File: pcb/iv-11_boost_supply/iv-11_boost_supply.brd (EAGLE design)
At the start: 54.6 x 47 mm, 18 parts, among them IC1 LM555D, M1 IRF540

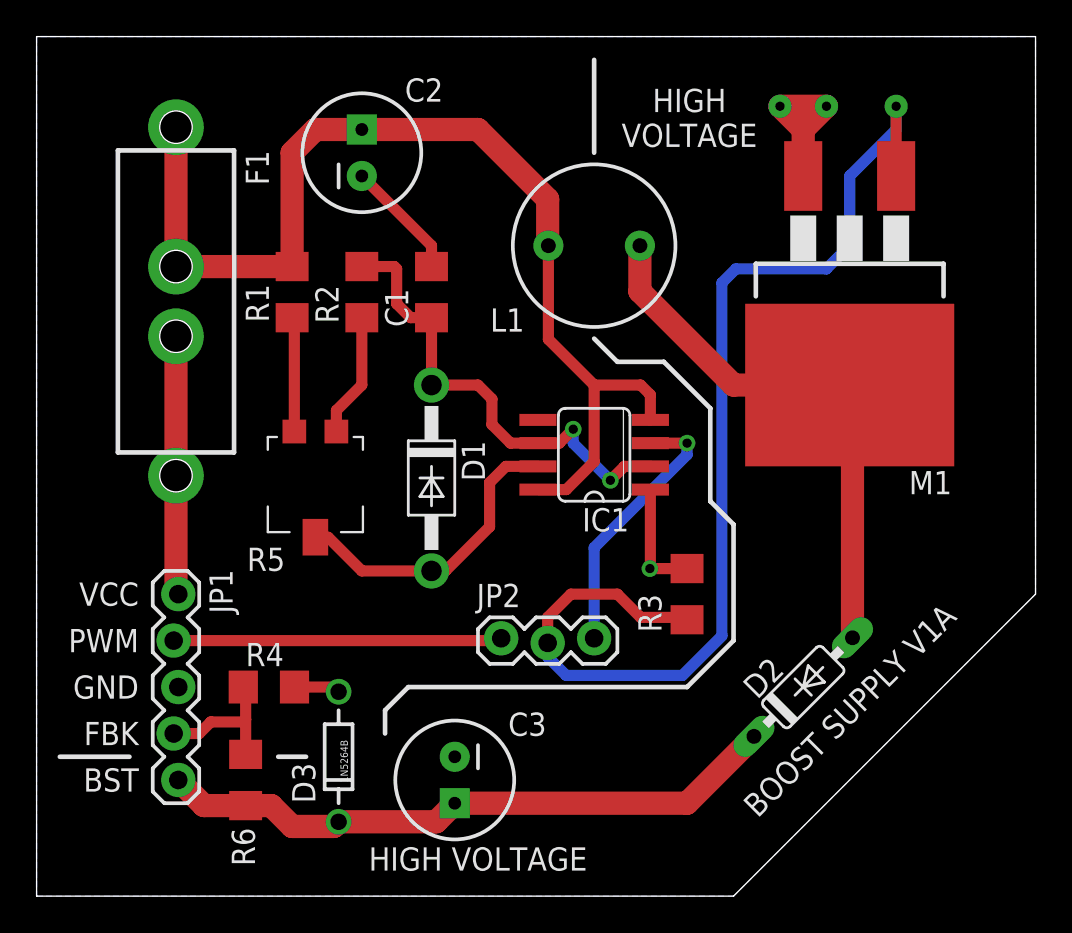
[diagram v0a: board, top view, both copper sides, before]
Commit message: Working on rev B of the boost supply board
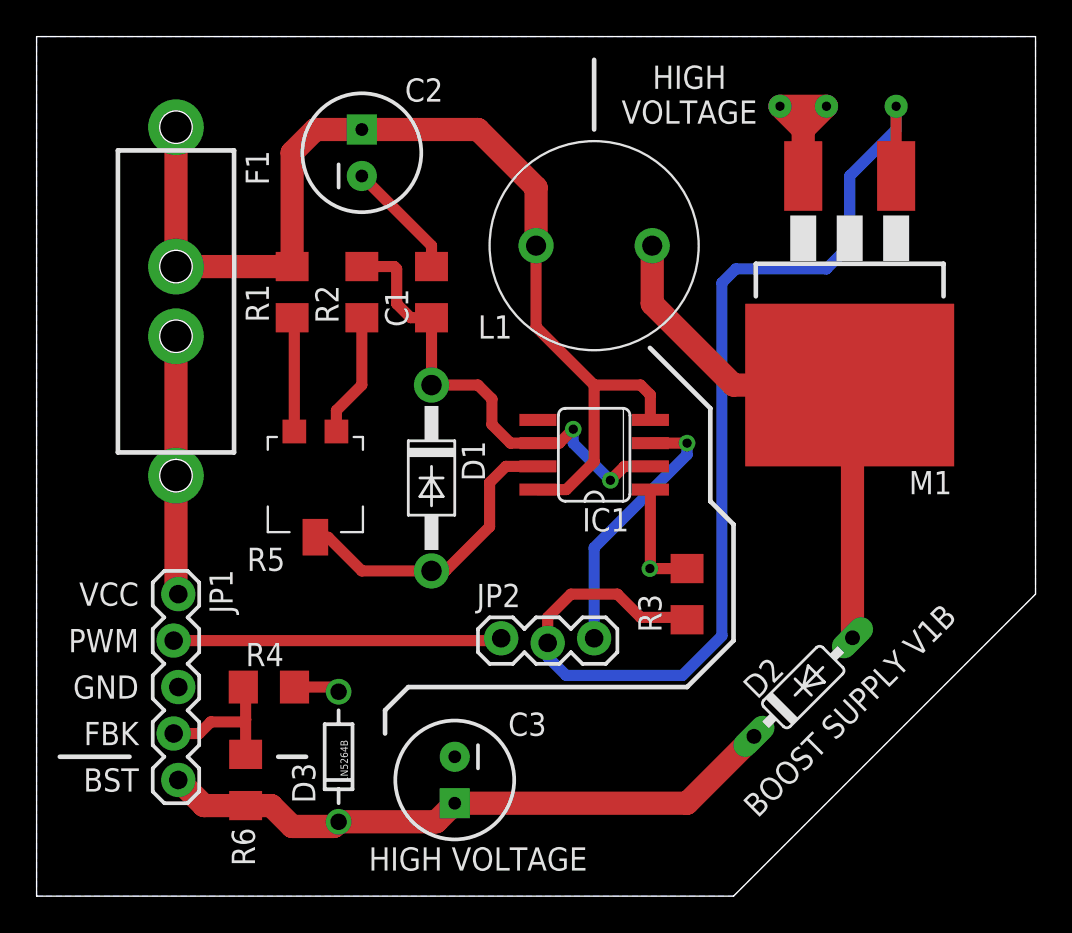
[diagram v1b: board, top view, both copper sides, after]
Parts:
- L1: device SparkFun-Passives:RLB0912 -> boztalay:INDUCTOR-PTH-13MM
- turned L1 to 0 degrees
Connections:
- net N$4: now also L1.B; no longer L1.2
- net VCC_PRC: now also L1.A; no longer L1.1
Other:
- board text added: "BOOST SUPPLY V1B"
- board text removed: "BOOST SUPPLY V1A"
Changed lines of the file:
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@@
 <wire x1="38.1" y1="20.32" x2="36.83" y2="21.59" width="0.254" layer="21"/>
 <wire x1="36.83" y1="21.59" x2="36.83" y2="26.67" width="0.254" layer="21"/>
-<wire x1="36.83" y1="26.67" x2="34.29" y2="29.21" width="0.254" layer="21"/>
-<wire x1="34.29" y1="29.21" x2="31.75" y2="29.21" width="0.254" layer="21"/>
-<wire x1="31.75" y1="29.21" x2="30.48" y2="30.48" width="0.254" layer="21"/>
-<wire x1="30.48" y1="40.64" x2="30.48" y2="45.72" width="0.254" layer="21"/>
+<wire x1="36.83" y1="26.67" x2="33.528" y2="29.972" width="0.254" layer="21"/>
+<wire x1="30.48" y1="41.91" x2="30.48" y2="45.72" width="0.254" layer="21"/>
 <wire x1="0" y1="0" x2="38.1" y2="0" width="0" layer="20"/>
 <wire x1="38.1" y1="0" x2="54.61" y2="16.51" width="0" layer="20"/>
@@
 <text x="5.588" y="8.89" size="1.27" layer="21" font="vector" ratio="11" align="center-right">FBK</text>
 <text x="5.588" y="6.35" size="1.27" layer="21" font="vector" ratio="11" align="center-right">BST</text>
-<text x="35.687" y="42.545" size="1.27" layer="21" font="vector" ratio="11" align="center">HIGH
+<text x="35.687" y="43.815" size="1.27" layer="21" font="vector" ratio="11" align="center">HIGH
 VOLTAGE</text>
 <text x="24.13" y="2.032" size="1.27" layer="21" font="vector" ratio="11" align="center">HIGH VOLTAGE</text>
-<text x="44.45" y="10.16" size="1.27" layer="21" font="vector" ratio="11" rot="R45" align="center">BOOST SUPPLY V1A</text>
+<text x="44.45" y="10.16" size="1.27" layer="21" font="vector" ratio="11" rot="R45" align="center">BOOST SUPPLY V1B</text>
 </plain>
 <attributes>
@@
 <attribute name="VALUE" x="17.018" y="6.223" size="0.4064" layer="21" rot="R90"/>
 </element>
-<element name="F1" library="boztalay" package="1AG-1/4X5/8-FUSE" value="2A/32V" x="7.62" y="32.512" rot="R270"/>
+<element name="F1" library="boztalay" package="1AG-1/4X5/8-FUSE" value="2A/32V" x="7.62" y="32.512" rot="R270">
+<attribute name="RATING" value="" x="7.62" y="32.512" size="1.778" layer="27" rot="R270" display="off"/>
+</element>
 <element name="IC1" library="adafruit" package="SO08" value="LM555D" x="30.48" y="24.13" rot="R90"/>
 <element name="JP1" library="SparkFun-Connectors" package="1X05_LOCK" value="" x="7.62" y="16.51" rot="R270"/>
 <element name="JP2" library="SparkFun-Connectors" package="1X03_LOCK" value="" x="25.4" y="13.97"/>
-<element name="L1" library="SparkFun-Passives" package="RLB0912" value="2200uH" x="30.48" y="35.56" smashed="yes" rot="R180">
-<attribute name="VALUE" x="32.385" y="38.608" size="0.8128" layer="27" rot="R180"/>
-<attribute name="NAME" x="26.67" y="32.131" size="1.27" layer="25" rot="R180"/>
-</element>
 <element name="M1" library="boztalay" package="D2PACK" value="IRF540" x="44.45" y="30.48" rot="R180"/>
 <element name="R1" library="SparkFun-Passives" package="1206" value="100" x="13.97" y="33.02" smashed="yes" rot="R90">
@@
 </element>
 <element name="D2" library="adafruit" package="DO35-7" value="MBR160" x="41.91" y="11.43" rot="R45"/>
+<element name="L1" library="boztalay" package="INDUCTOR-PTH-13MM" value="2200uH" x="30.48" y="35.56" smashed="yes">
+<attribute name="VALUE" x="35.56" y="30.48" size="1.27" layer="27"/>
+<attribute name="NAME" x="24.13" y="30.48" size="1.27" layer="25"/>
+</element>
 </elements>
 <signals>
@@
 </signal>
 <signal name="N$4">
-<contactref element="L1" pad="2"/>
 <contactref element="M1" pad="2"/>
 <contactref element="D2" pad="A"/>
 <wire x1="44.604075" y1="14.124075" x2="44.604075" y2="27.785925" width="1.27" layer="1"/>
 <wire x1="44.604075" y1="27.785925" x2="44.45" y2="27.94" width="1.27" layer="1"/>
-<wire x1="32.9819" y1="35.56" x2="32.9819" y2="33.0581" width="1.27" layer="1"/>
-<wire x1="32.9819" y1="33.0581" x2="38.1" y2="27.94" width="1.27" layer="1"/>
 <wire x1="38.1" y1="27.94" x2="44.45" y2="27.94" width="1.27" layer="1"/>
+<contactref element="L1" pad="B"/>
+<wire x1="33.655" y1="35.56" x2="33.655" y2="32.385" width="1.27" layer="1"/>
+<wire x1="33.655" y1="32.385" x2="38.1" y2="27.94" width="1.27" layer="1"/>
 </signal>
 <signal name="VCC_PRC">
@@
 <contactref element="R1" pad="2"/>
 <contactref element="IC1" pad="4"/>
-<contactref element="L1" pad="1"/>
 <contactref element="IC1" pad="8"/>
 <wire x1="7.62" y1="42.037" x2="7.62" y2="34.417" width="1.27" layer="1"/>
@@
 <wire x1="15.24" y1="41.91" x2="17.78" y2="41.91" width="1.27" layer="1"/>
 <wire x1="17.78" y1="41.91" x2="24.13" y2="41.91" width="1.27" layer="1"/>
-<wire x1="24.13" y1="41.91" x2="27.94" y2="38.1" width="1.27" layer="1"/>
-<wire x1="27.94" y1="38.1" x2="27.94" y2="35.5981" width="1.27" layer="1"/>
-<wire x1="27.94" y1="35.5981" x2="27.9781" y2="35.56" width="1.27" layer="1"/>
-<wire x1="27.9781" y1="35.56" x2="27.9781" y2="30.4419" width="0.6096" layer="1"/>
-<wire x1="27.9781" y1="30.4419" x2="30.48" y2="27.94" width="0.6096" layer="1"/>
 <wire x1="30.48" y1="27.94" x2="33.02" y2="27.94" width="0.6096" layer="1"/>
 <wire x1="33.5534" y1="26.035" x2="33.5534" y2="27.4066" width="0.6096" layer="1"/>
@@
 <wire x1="30.48" y1="23.749" x2="28.956" y2="22.225" width="0.6096" layer="1"/>
 <wire x1="28.956" y1="22.225" x2="27.4066" y2="22.225" width="0.6096" layer="1"/>
+<contactref element="L1" pad="A"/>
+<wire x1="24.13" y1="41.91" x2="27.305" y2="38.735" width="1.27" layer="1"/>
+<wire x1="27.305" y1="38.735" x2="27.305" y2="35.56" width="1.27" layer="1"/>
+<wire x1="27.305" y1="35.56" x2="27.305" y2="31.115" width="0.6096" layer="1"/>
+<wire x1="27.305" y1="31.115" x2="30.48" y2="27.94" width="0.6096" layer="1"/>
 </signal>
 </signals>

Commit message: Finished up rev B of the boost supply board, but the layout still needs to be tested
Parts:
- C3: device SparkFun-Passives:CPOL-RADIAL-100UF-25V -> boztalay:POLAR-CAP-PTH-10MM
- D2: device adafruit:DO35-7 -> adafruit:DO41-10
- moved C3 5.08 mm to (27.9, 6.35), turned to 90 degrees
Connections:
- net BST: now also C3.A; no longer C3.1
- net GND: now also C3.B; no longer C3.2
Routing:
- net BST: track 34.6 -> 33.4 mm
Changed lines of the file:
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@@
 <text x="35.687" y="43.815" size="1.27" layer="21" font="vector" ratio="11" align="center">HIGH
 VOLTAGE</text>
-<text x="24.13" y="2.032" size="1.27" layer="21" font="vector" ratio="11" align="center">HIGH VOLTAGE</text>
+<text x="16.51" y="2.032" size="1.27" layer="21" font="vector" ratio="11" align="center">HIGH VOLTAGE</text>
 <text x="44.45" y="10.16" size="1.27" layer="21" font="vector" ratio="11" rot="R45" align="center">BOOST SUPPLY V1B</text>
 </plain>
@@
 </class>
 </classes>
-<designrules name="default">
+<designrules name="default *">
 <description language="de">&lt;b&gt;EAGLE Design Rules&lt;/b&gt;
 &lt;p&gt;
@@
 <param name="mtCopper" value="0.035mm 0.035mm 0.035mm 0.035mm 0.035mm 0.035mm 0.035mm 0.035mm 0.035mm 0.035mm 0.035mm 0.035mm 0.035mm 0.035mm 0.035mm 0.035mm"/>
 <param name="mtIsolate" value="1.5mm 0.15mm 0.2mm 0.15mm 0.2mm 0.15mm 0.2mm 0.15mm 0.2mm 0.15mm 0.2mm 0.15mm 0.2mm 0.15mm 0.2mm"/>
-<param name="mdWireWire" value="8mil"/>
-<param name="mdWirePad" value="8mil"/>
-<param name="mdWireVia" value="8mil"/>
-<param name="mdPadPad" value="8mil"/>
-<param name="mdPadVia" value="8mil"/>
-<param name="mdViaVia" value="8mil"/>
-<param name="mdSmdPad" value="8mil"/>
-<param name="mdSmdVia" value="8mil"/>
-<param name="mdSmdSmd" value="8mil"/>
+<param name="mdWireWire" value="10mil"/>
+<param name="mdWirePad" value="10mil"/>
+<param name="mdWireVia" value="10mil"/>
+<param name="mdPadPad" value="10mil"/>
+<param name="mdPadVia" value="10mil"/>
+<param name="mdViaVia" value="10mil"/>
+<param name="mdSmdPad" value="10mil"/>
+<param name="mdSmdVia" value="10mil"/>
+<param name="mdSmdSmd" value="10mil"/>
 <param name="mdViaViaSameLayer" value="8mil"/>
 <param name="mnLayersViaInSmd" value="2"/>
@@
 <param name="srMinRoundness" value="0mil"/>
 <param name="srMaxRoundness" value="0mil"/>
-<param name="slThermalIsolate" value="10mil"/>
+<param name="slThermalIsolate" value="8mil"/>
 <param name="slThermalsForVias" value="0"/>
 <param name="dpMaxLengthDifference" value="10mm"/>
@@
 <attribute name="NAME" x="22.225" y="44.704" size="1.27" layer="25" rot="R180"/>
 </element>
-<element name="C3" library="SparkFun-Passives" package="CPOL-RADIAL-100UF-25V" value="100uF" x="22.86" y="6.35" smashed="yes" rot="R270">
-<attribute name="VALUE" x="18.542" y="8.255" size="0.8128" layer="27" rot="R270"/>
-<attribute name="NAME" x="25.781" y="8.763" size="1.27" layer="25"/>
-</element>
-<element name="D1" library="adafruit" package="DO41-10" value="1N4004" x="21.59" y="22.86" rot="R270"/>
+<element name="D1" library="adafruit" package="DO41-10" value="1N4004" x="21.59" y="22.86" smashed="yes" rot="R270">
+<attribute name="NAME" x="18.669" y="22.987" size="1.27" layer="25" ratio="10" rot="R270"/>
+<attribute name="VALUE" x="18.796" y="24.892" size="1.27" layer="27" ratio="10" rot="R270"/>
+</element>
 <element name="D3" library="SparkFun-DiscreteSemi" package="DIODE-ZENER" value="1N5264B" x="16.51" y="7.62" smashed="yes" rot="R90">
-<attribute name="NAME" x="15.24" y="5.08" size="1.27" layer="25" rot="R90"/>
-<attribute name="VALUE" x="17.018" y="6.223" size="0.4064" layer="21" rot="R90"/>
+<attribute name="NAME" x="19.05" y="5.08" size="1.27" layer="25" rot="R90"/>
 </element>
 <element name="F1" library="boztalay" package="1AG-1/4X5/8-FUSE" value="2A/32V" x="7.62" y="32.512" rot="R270">
@@
 </element>
 <element name="R6" library="SparkFun-Passives" package="1206" value="110k" x="11.43" y="6.35" smashed="yes" rot="R90">
-<attribute name="NAME" x="11.938" y="1.651" size="1.27" layer="25" rot="R90"/>
+<attribute name="NAME" x="8.001" y="3.302" size="1.27" layer="25"/>
 <attribute name="VALUE" x="12.954" y="4.953" size="0.4064" layer="27" rot="R90"/>
 </element>
-<element name="D2" library="adafruit" package="DO35-7" value="MBR160" x="41.91" y="11.43" rot="R45"/>
 <element name="L1" library="boztalay" package="INDUCTOR-PTH-13MM" value="2200uH" x="30.48" y="35.56" smashed="yes">
 <attribute name="VALUE" x="35.56" y="30.48" size="1.27" layer="27"/>
 <attribute name="NAME" x="24.13" y="30.48" size="1.27" layer="25"/>
 </element>
+<element name="C3" library="boztalay" package="POLAR-CAP-PTH-10MM" value="100uF" x="27.94" y="6.35" smashed="yes" rot="R90">
+<attribute name="VALUE" x="31.75" y="11.43" size="1.27" layer="27" rot="R90" align="top-left"/>
+<attribute name="NAME" x="21.59" y="8.89" size="1.27" layer="25"/>
+</element>
+<element name="D2" library="adafruit" package="DO41-10" value="MBR160" x="41.91" y="11.43" rot="R45"/>
 </elements>
 <signals>
@@
 <contactref element="M1" pad="3"/>
 <contactref element="C2" pad="2"/>
-<contactref element="C3" pad="2"/>
 <contactref element="D3" pad="P$2"/>
 <contactref element="R4" pad="2"/>
 <contactref element="JP1" pad="3"/>
-<via x="40.64" y="43.18" extent="1-16" drill="0.508" diameter="1.27"/>
-<via x="43.18" y="43.18" extent="1-16" drill="0.508" diameter="1.27"/>
-<via x="33.528" y="17.907" extent="1-16" drill="0.508"/>
+<via x="40.64" y="43.18" extent="1-16" drill="0.6096" diameter="1.27"/>
+<via x="43.18" y="43.18" extent="1-16" drill="0.6096" diameter="1.27"/>
+<via x="33.528" y="17.907" extent="1-16" drill="0.6096"/>
 <wire x1="21.59" y1="34.42" x2="21.59" y2="35.56" width="0.6096" layer="1"/>
 <wire x1="21.59" y1="35.56" x2="17.78" y2="39.37" width="0.6096" layer="1"/>
@@
 <wire x1="41.91" y1="41.91" x2="41.91" y2="39.37" width="1.27" layer="1"/>
 <wire x1="40.64" y1="43.18" x2="41.91" y2="41.91" width="1.27" layer="1"/>
+<contactref element="C3" pad="B"/>
 </signal>
 <signal name="FBK">
@@
 <signal name="BST">
 <contactref element="JP1" pad="5"/>
-<contactref element="C3" pad="1"/>
 <contactref element="D3" pad="P$1"/>
-<contactref element="D2" pad="C"/>
 <contactref element="R6" pad="1"/>
 <wire x1="11.43" y1="4.95" x2="12.83" y2="4.95" width="1.27" layer="1"/>
@@
 <wire x1="11.43" y1="4.95" x2="9.147" y2="4.95" width="1.27" layer="1"/>
 <wire x1="9.147" y1="4.95" x2="7.747" y2="6.35" width="1.27" layer="1"/>
-<wire x1="16.51" y1="4.064" x2="21.844" y2="4.064" width="1.27" layer="1"/>
-<wire x1="21.844" y1="4.064" x2="22.86" y2="5.08" width="1.27" layer="1"/>
-<wire x1="22.86" y1="5.08" x2="35.56" y2="5.08" width="1.27" layer="1"/>
-<wire x1="35.56" y1="5.08" x2="39.215921875" y2="8.735921875" width="1.27" layer="1"/>
+<contactref element="C3" pad="A"/>
+<wire x1="34.661975" y1="4.181975" x2="33.76395" y2="3.81" width="1.27" layer="1" curve="-45"/>
+<wire x1="33.76395" y1="3.81" x2="27.94" y2="3.81" width="1.27" layer="1"/>
+<wire x1="27.94" y1="3.81" x2="17.123209375" y2="3.81" width="1.27" layer="1"/>
+<wire x1="17.123209375" y1="3.81" x2="16.51" y2="4.064" width="1.27" layer="1" curve="-45"/>
+<contactref element="D2" pad="C"/>
+<wire x1="34.661975" y1="4.181975" x2="38.317896875" y2="7.837896875" width="1.27" layer="1"/>
 </signal>
 <signal name="N$1">
@@
 <wire x1="24.892" y1="25.781" x2="25.908" y2="24.765" width="0.6096" layer="1"/>
 <wire x1="25.908" y1="24.765" x2="27.4066" y2="24.765" width="0.6096" layer="1"/>
-<via x="29.337" y="25.527" extent="1-16" drill="0.508"/>
-<via x="31.369" y="22.733" extent="1-16" drill="0.508"/>
+<via x="29.337" y="25.527" extent="1-16" drill="0.6096"/>
+<via x="31.369" y="22.733" extent="1-16" drill="0.6096"/>
 <wire x1="29.337" y1="25.527" x2="29.337" y2="24.765" width="0.6096" layer="16"/>
 <wire x1="29.337" y1="24.765" x2="31.369" y2="22.733" width="0.6096" layer="16"/>
@@
 <contactref element="IC1" pad="3"/>
 <contactref element="JP2" pad="3"/>
-<via x="35.56" y="24.765" extent="1-16" drill="0.508"/>
+<via x="35.56" y="24.765" extent="1-16" drill="0.6096"/>
 <wire x1="35.56" y1="24.765" x2="35.56" y2="24.13" width="0.6096" layer="16"/>
 <wire x1="33.5534" y1="24.765" x2="35.56" y2="24.765" width="0.6096" layer="1"/>
@@
 <contactref element="M1" pad="1"/>
 <contactref element="R3" pad="2"/>
-<via x="46.99" y="43.18" extent="1-16" drill="0.508" diameter="1.27"/>
+<via x="46.99" y="43.18" extent="1-16" drill="0.6096" diameter="1.27"/>
 <wire x1="46.99" y1="43.18" x2="46.99" y2="41.91" width="0.6096" layer="16"/>
 <wire x1="46.99" y1="41.91" x2="44.45" y2="39.37" width="0.6096" layer="16"/>
@@
 <signal name="N$4">
 <contactref element="M1" pad="2"/>
-<contactref element="D2" pad="A"/>
-<wire x1="44.604075" y1="14.124075" x2="44.604075" y2="27.785925" width="1.27" layer="1"/>
 <wire x1="44.604075" y1="27.785925" x2="44.45" y2="27.94" width="1.27" layer="1"/>
 <wire x1="38.1" y1="27.94" x2="44.45" y2="27.94" width="1.27" layer="1"/>
@@
 <wire x1="33.655" y1="35.56" x2="33.655" y2="32.385" width="1.27" layer="1"/>
 <wire x1="33.655" y1="32.385" x2="38.1" y2="27.94" width="1.27" layer="1"/>
+<contactref element="D2" pad="A"/>
+<wire x1="45.5021" y1="15.0221" x2="45.5021" y2="26.36185" width="1.27" layer="1"/>
+<wire x1="45.5021" y1="26.36185" x2="45.130125" y2="27.259875" width="1.27" layer="1" curve="45"/>
+<wire x1="45.130125" y1="27.259875" x2="44.45" y2="27.94" width="1.27" layer="1"/>
 </signal>
 <signal name="VCC_PRC">
